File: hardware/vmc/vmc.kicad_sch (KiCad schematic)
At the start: 35 parts, among them J1 Conn_01x05_Pin, J2 push button, J3 BUS, M1 Motor_DC, Q1 BSS123, U1 SHT31-DIS, U2 PIC18F05Q40, U3 DRV8832DGQR, U4 MCP2003B, U5 uA7805

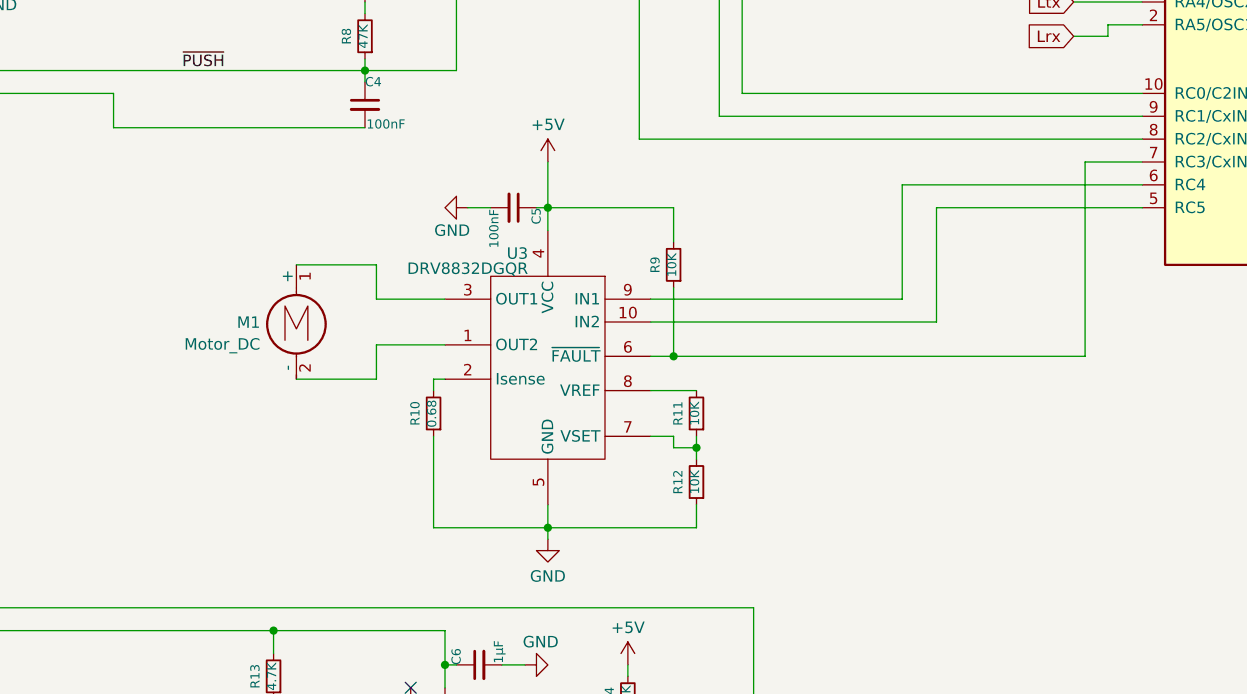
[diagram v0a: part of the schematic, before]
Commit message: vnc: Remplace le driver DRV8832DGQR (obsolete) par un MAX22201
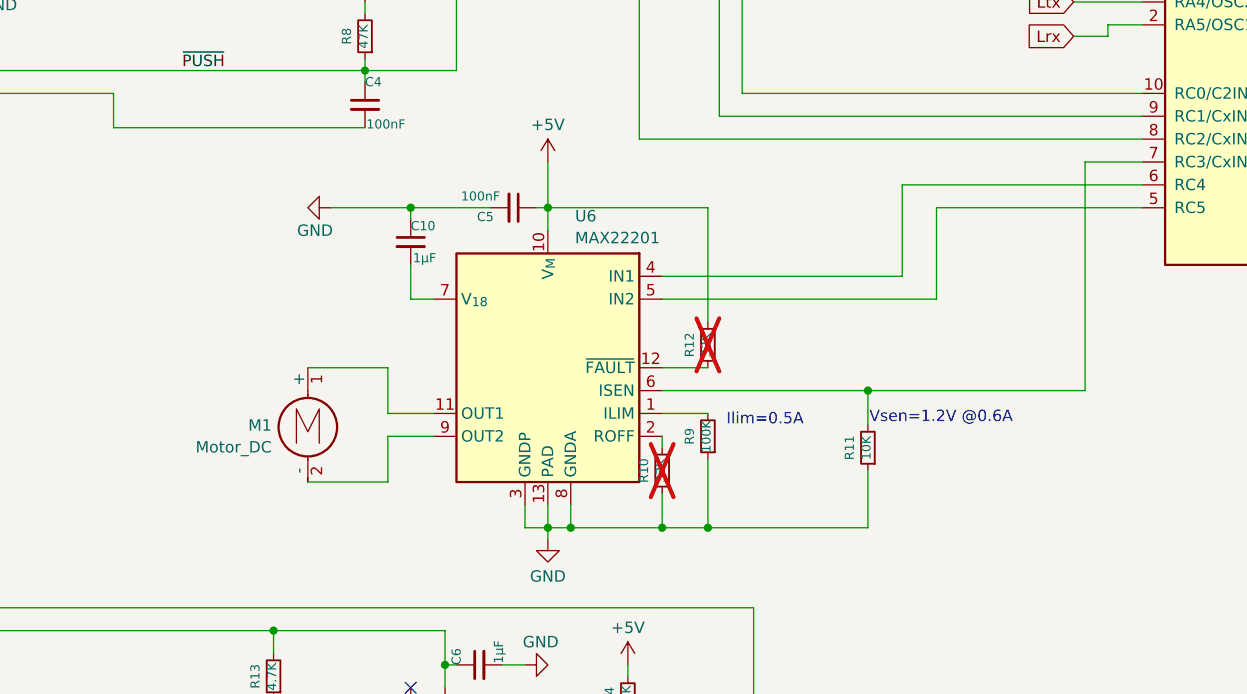
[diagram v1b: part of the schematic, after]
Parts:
- removed U3: DRV8832DGQR, Package_SO:MSOP-10-1EP_3x3mm_P0.5mm_EP2.2x3.1mm_Mask1.83x1.89mm, symbol motor-local:DRV8832
- added C10: 1µF, Capacitor_SMD:C_0603_1608Metric_Pad1.08x0.95mm_HandSolder, symbol Device:C_Small
- added U6: MAX22201, Package_DFN_QFN:Maxim_TDFN-12-1EP_3x3mm_P0.5mm_EP1.7x2.5mm, symbol Driver_Motor:MAX22201
- R10: value 0.68 -> 33K; footprint Resistor_SMD:R_1206_3216Metric_Pad1.30x1.75mm_HandSolder -> Resistor_SMD:R_0805_2012Metric_Pad1.20x1.40mm_HandSolder; P/N WW12PR680FTL -> stock; now not fitted; now left out of the parts list
- R12: value 10K -> 33K; now not fitted; now left out of the parts list
- R9: value 10K -> 100K
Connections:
- net +5V: now also R12.2, U6.10 (V_{M}); no longer R9.2
- net GND: now also R11.1, R9.1, C10.1, U6.13 (PAD), U6.3 (GNDP), U6.8 (GNDA); no longer R12.1
- net at R11.2: now also U2.7 (RC3/CxIN3-), U6.6 (ISEN)
- net at U2.5 (RC5): now also U6.5 (IN2)
- net at U2.6 (RC4): now also U6.4 (IN1)
- net at R10.2: now also U6.2 (ROFF)
- net at M1.2 (-): now also U6.9 (OUT2)
- net at M1.1 (+): now also U6.11 (OUT1)
- new net: R9.2, U6.1 (ILIM)
- new net: C10.2, U6.7 (V_{18})
- new net: R12.1, U6.12 (~{FAULT})
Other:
- note added: "Ilim=0.5A"
- note added: "Vsen=1.2V @0.6A"
- moved on the sheet: M1

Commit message: vmc: swap button/LED pins to limit damage on accidental connect to LIN bus. Name remaining connector signals
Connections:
- net GND: now also J2.1 (Pin_1); no longer J2.4 (Pin_4)
- net ~{PUSH}: now also J2.2 (Pin_2); no longer J2.3 (Pin_3)
- net LED-: now reaches D1.1 (K), Q1.3 (D)
- net LED-: now also J2.4 (Pin_4); no longer J2.1 (Pin_1)
- net LED+: now reaches R4.2
- net LED+: now also J2.3 (Pin_3); no longer J2.2 (Pin_2)
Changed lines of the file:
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@@
 		)
 	)
+	(label "LED-"
+		(at 80.01 46.99 0)
+		(fields_autoplaced yes)
+		(effects
+			(font
+				(size 1.27 1.27)
+			)
+			(justify left bottom)
+		)
+	)
+	(label "LED+"
+		(at 73.66 50.8 90)
+		(fields_autoplaced yes)
+		(effects
+			(font
+				(size 1.27 1.27)
+			)
+			(justify left bottom)
+		)
+	)
 	(label "PGC"
 		(at 215.9 57.15 0)
@@
 	(symbol
 		(lib_id "Connector:Conn_01x04_Pin")
-		(at 63.5 69.85 0)
+		(at 63.5 72.39 0)
+		(mirror x)
 		(unit 1)
 		(exclude_from_sim no)
@@
 		(on_board yes)
 		(dnp no)
-		(fields_autoplaced yes)
 		(property "Reference" "J2"
-			(at 64.135 62.23 0)
+			(at 64.135 80.01 0)
 			(effects
 				(font
@@
 		)
 		(property "Value" "push button"
-			(at 64.135 64.77 0)
+			(at 64.135 77.47 0)
 			(effects
 				(font
@@
 		)
 		(property "Footprint" "conn-local:Molex Pico-SPOX-4_90"
-			(at 63.5 69.85 0)
+			(at 63.5 72.39 0)
 			(effects
 				(font
@@
 		)
 		(property "Datasheet" "~"
-			(at 63.5 69.85 0)
+			(at 63.5 72.39 0)
 			(effects
 				(font
@@
 		)
 		(property "Description" "Generic connector, single row, 01x04, script generated"
-			(at 63.5 69.85 0)
+			(at 63.5 72.39 0)
 			(effects
 				(font
@@
 		)
 		(property "P/N" "87438-0443"
-			(at 63.5 69.85 0)
+			(at 63.5 72.39 0)
 			(effects
 				(font

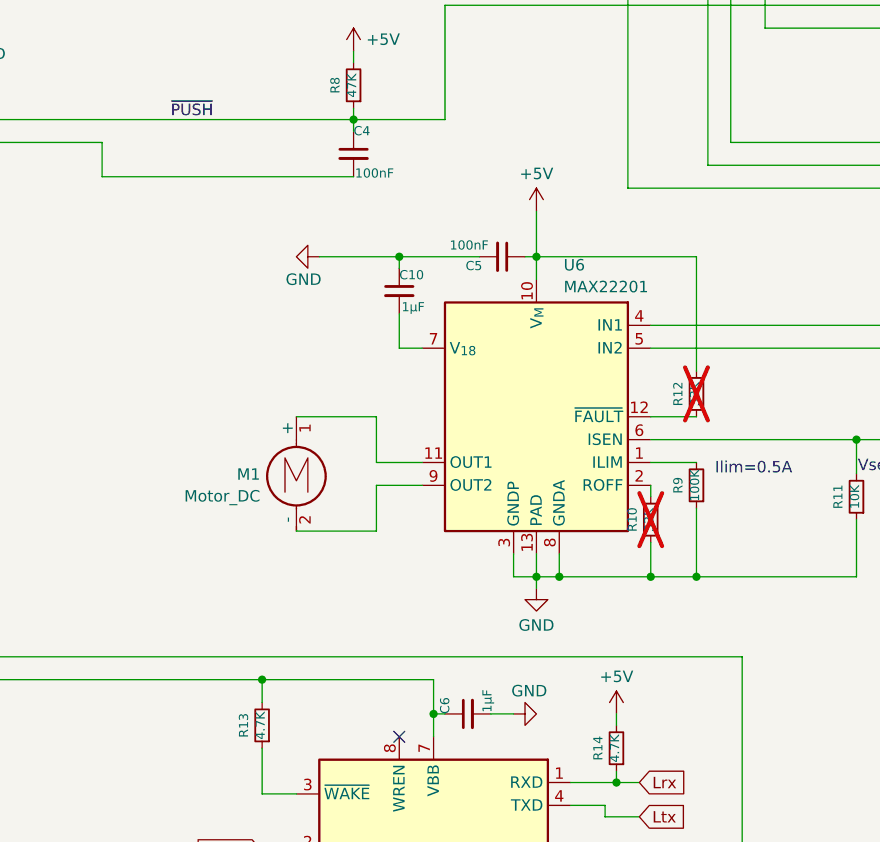
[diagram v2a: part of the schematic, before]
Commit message: Alimente le driver max22201 en 12V; le courant moteur est limité par le driver en PWM et cela permet de tirer un peu moins sur l'alim (et le régulateur 5V)
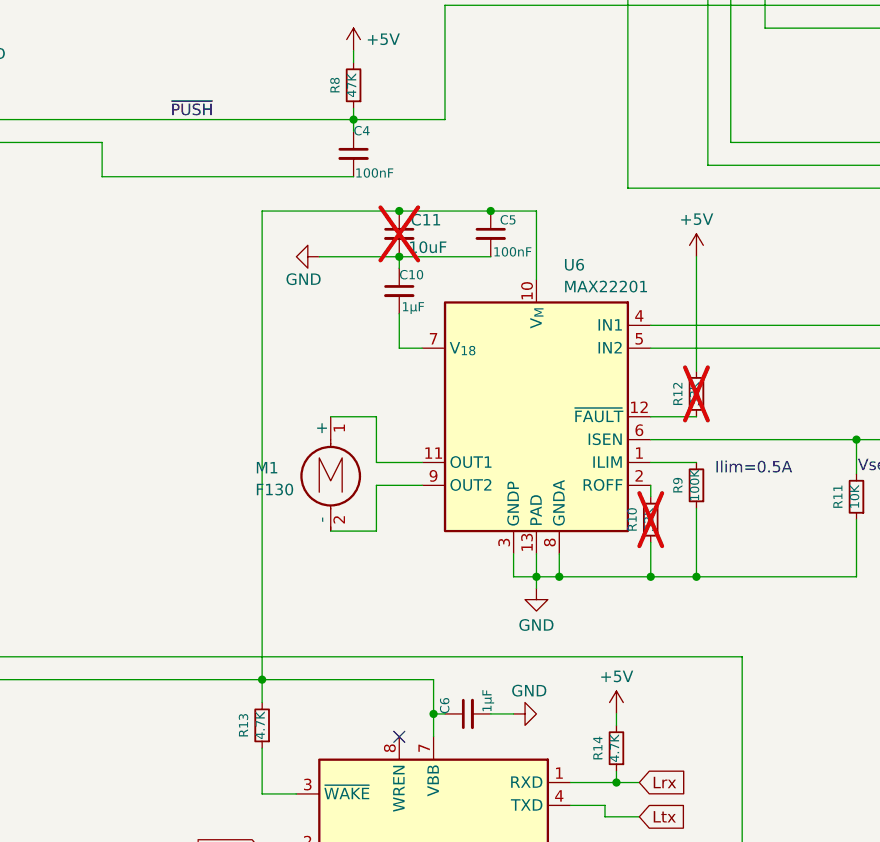
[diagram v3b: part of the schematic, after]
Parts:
- added C11: 10uF, Capacitor_SMD:C_1210_3225Metric_Pad1.33x2.70mm_HandSolder, symbol Device:C_Small
- M1: value Motor_DC -> F130
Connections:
- net +12V: now also C5.1, U6.10 (V_{M}), C11.1
- net +5V: no longer C5.1, U6.10 (V_{M})
- net GND: now also C11.2
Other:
- moved on the sheet: C5, M1
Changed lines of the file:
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@@
 	)
 	(junction
+		(at 147.32 82.55)
+		(diameter 0)
+		(color 0 0 0 0)
+	)
+	(junction
 		(at 142.24 72.39)
 		(diameter 0)
@@
 	)
 	(junction
+		(at 157.48 82.55)
+		(diameter 0)
+		(color 0 0 0 0)
+	)
+	(junction
 		(at 151.13 170.18)
 		(diameter 0)
@@
 	)
 	(junction
-		(at 162.56 87.63)
-		(diameter 0)
-		(color 0 0 0 0)
-	)
-	(junction
 		(at 73.66 170.18)
 		(diameter 0)
@@
 	(wire
 		(pts
-			(xy 144.78 105.41) (xy 135.89 105.41)
+			(xy 144.78 105.41) (xy 139.7 105.41)
 		)
 		(stroke
@@
 	(wire
 		(pts
-			(xy 162.56 87.63) (xy 180.34 87.63)
-		)
-		(stroke
-			(width 0)
-			(type default)
-		)
-	)
-	(wire
-		(pts
 			(xy 201.93 20.32) (xy 201.93 25.4)
 		)
@@
 	(wire
 		(pts
-			(xy 162.56 87.63) (xy 162.56 90.17)
-		)
-		(stroke
-			(width 0)
-			(type default)
-		)
-	)
-	(wire
-		(pts
 			(xy 68.58 67.31) (xy 76.2 67.31)
 		)
@@
 	(wire
 		(pts
-			(xy 162.56 82.55) (xy 162.56 87.63)
+			(xy 162.56 82.55) (xy 162.56 90.17)
 		)
 		(stroke
@@
 	(wire
 		(pts
-			(xy 144.78 118.11) (xy 135.89 118.11)
+			(xy 144.78 118.11) (xy 139.7 118.11)
 		)
 		(stroke
@@
 	(wire
 		(pts
+			(xy 147.32 82.55) (xy 157.48 82.55)
+		)
+		(stroke
+			(width 0)
+			(type default)
+		)
+	)
+	(wire
+		(pts
 			(xy 185.42 156.21) (xy 168.91 156.21)
 		)
@@
 	(wire
 		(pts
+			(xy 132.08 134.62) (xy 132.08 82.55)
+		)
+		(stroke
+			(width 0)
+			(type default)
+		)
+	)
+	(wire
+		(pts
 			(xy 175.26 123.19) (xy 165.1 123.19)
 		)
@@
 	(wire
 		(pts
-			(xy 175.26 113.03) (xy 175.26 114.3)
+			(xy 157.48 82.55) (xy 162.56 82.55)
 		)
 		(stroke
@@
 	(wire
 		(pts
-			(xy 132.08 153.67) (xy 135.89 153.67)
+			(xy 175.26 113.03) (xy 175.26 114.3)
 		)
 		(stroke
@@
 	(wire
 		(pts
-			(xy 162.56 87.63) (xy 161.29 87.63)
+			(xy 132.08 153.67) (xy 135.89 153.67)
 		)
 		(stroke
@@
 	(wire
 		(pts
-			(xy 156.21 87.63) (xy 147.32 87.63)
+			(xy 147.32 87.63) (xy 157.48 87.63)
 		)
 		(stroke
@@
 	(wire
 		(pts
+			(xy 132.08 82.55) (xy 147.32 82.55)
+		)
+		(stroke
+			(width 0)
+			(type default)
+		)
+	)
+	(wire
+		(pts
 			(xy 228.6 82.55) (xy 222.25 82.55)
 		)
@@
 	(symbol
 		(lib_id "power:+5V")
-		(at 162.56 82.55 0)
+		(at 180.34 87.63 0)
 		(unit 1)
 		(exclude_from_sim no)
@@
 		(fields_autoplaced yes)
 		(property "Reference" "#PWR012"
-			(at 162.56 86.36 0)
+			(at 180.34 91.44 0)
 			(effects
 				(font
@@
 		)
 		(property "Value" "+5V"
-			(at 162.56 78.4169 0)
+			(at 180.34 83.4969 0)
 			(effects
 				(font
@@
 		)
 		(property "Footprint" ""
-			(at 162.56 82.55 0)
+			(at 180.34 87.63 0)
 			(effects
 				(font
@@
 		)
 		(property "Datasheet" ""
-			(at 162.56 82.55 0)
+			(at 180.34 87.63 0)
 			(effects
 				(font
@@
 		)
 		(property "Description" "Power symbol creates a global label with name \"+5V\""
-			(at 162.56 82.55 0)
+			(at 180.34 87.63 0)
 			(effects
 				(font
@@
 		)
 		(property "P/N" ""
-			(at 162.56 82.55 0)
+			(at 180.34 87.63 0)
 			(effects
 				(font
@@
 	(symbol
 		(lib_id "Device:C_Small")
-		(at 158.75 87.63 270)
+		(at 157.48 85.09 0)
 		(unit 1)
 		(exclude_from_sim no)
@@
 		(dnp no)
 		(property "Reference" "C5"
-			(at 154.686 88.646 90)
+			(at 158.496 83.566 0)
 			(effects
 				(font
@@
 		)
 		(property "Value" "100nF"
-			(at 152.908 86.36 90)
+			(at 157.734 87.122 0)
 			(effects
 				(font
@@
 		)
 		(property "Footprint" "Capacitor_SMD:C_0603_1608Metric_Pad1.08x0.95mm_HandSolder"
-			(at 154.94 88.5952 0)
+			(at 158.4452 88.9 0)
 			(effects
 				(font
@@
 		)
 		(property "Datasheet" "~"
-			(at 158.75 87.63 0)
+			(at 157.48 85.09 0)
 			(effects
 				(font
@@
 		)
 		(property "Description" "Unpolarized capacitor, small symbol"
-			(at 158.75 87.63 0)
+			(at 157.48 85.09 0)
 			(effects
 				(font
@@
 		)
 		(property "P/N" "stock"
-			(at 158.75 87.63 0)
+			(at 157.48 85.09 0)
 			(effects
 				(font
@@
 	)
 	(symbol
+		(lib_id "Device:C_Small")
+		(at 147.32 85.09 0)
+		(unit 1)
+		(exclude_from_sim no)
+		(in_bom yes)
+		(on_board yes)
+		(dnp yes)
+		(property "Reference" "C11"
+			(at 148.59 83.566 0)
+			(effects
+				(font
+					(size 1.27 1.27)
+				)
+				(justify left)
+			)
+		)
+		(property "Value" "10uF"
+			(at 148.336 86.614 0)
+			(effects
+				(font
+					(size 1.27 1.27)
+				)
+				(justify left)
+			)
+		)
+		(property "Footprint" "Capacitor_SMD:C_1210_3225Metric_Pad1.33x2.70mm_HandSolder"
+			(at 147.32 85.09 0)
+			(effects
+				(font
+					(size 1.27 1.27)
+				)
+				(hide yes)
+			)
+		)
+		(property "Datasheet" "~"
+			(at 147.32 85.09 0)
+			(effects
+				(font
+					(size 1.27 1.27)
+				)
+				(hide yes)
+			)
+		)
+		(property "Description" "Unpolarized capacitor, small symbol"
+			(at 147.32 85.09 0)
+			(effects
+				(font
+					(size 1.27 1.27)
+				)
+				(hide yes)
+			)
+		)
+		(property "P/N" "C3225X5R1E106K250AA ou GCM32ER71E106KA57L (stock)"
+			(at 147.32 85.09 0)
+			(effects
+				(font
+					(size 1.27 1.27)
+				)
+				(hide yes)
+			)
+		)
+		(pin "1"
+		)
+		(pin "2"
+		)
+		(instances
+			(project "vmc"
+				(path "/c1528490-5337-42d0-8cda-ee7adecf27aa"
+					(reference "C11")
+					(unit 1)
+				)
+			)
+		)
+	)
+	(symbol
 		(lib_id "Device:R_Small")
 		(at 111.76 41.91 0)
@@
 	(symbol
 		(lib_id "Motor:Motor_DC")
-		(at 135.89 110.49 0)
+		(at 139.7 110.49 0)
 		(mirror y)
 		(unit 1)
@@
 		(on_board yes)
 		(dnp no)
-		(fields_autoplaced yes)
 		(property "Reference" "M1"
-			(at 131.8768 111.8178 0)
+			(at 131.318 111.1137 0)
 			(effects
 				(font
 					(size 1.27 1.27)
 				)
-				(justify left)
+				(justify right)
 			)
 		)
-		(property "Value" "Motor_DC"
-			(at 131.8768 114.2421 0)
+		(property "Value" "F130"
+			(at 131.318 113.538 0)
 			(effects
 				(font
 					(size 1.27 1.27)
 				)
-				(justify left)
+				(justify right)
 			)
 		)
 		(property "Footprint" "motors-local:F130"
-			(at 135.89 112.776 0)
+			(at 139.7 112.776 0)
 			(effects
 				(font
@@
 		)
 		(property "Datasheet" "~"
-			(at 135.89 112.776 0)
+			(at 139.7 112.776 0)
 			(effects
 				(font
@@
 		)
 		(property "Description" "DC Motor"
-			(at 135.89 110.49 0)
+			(at 139.7 110.49 0)
 			(effects
 				(font
@@
 		)
 		(property "P/N" "olimex F130"
-			(at 135.89 110.49 0)
+			(at 139.7 110.49 0)
 			(effects
 				(font
